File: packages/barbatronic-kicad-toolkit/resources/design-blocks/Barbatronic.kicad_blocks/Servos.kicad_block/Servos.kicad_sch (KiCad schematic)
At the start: 3 parts, among them J19 Conn_01x04

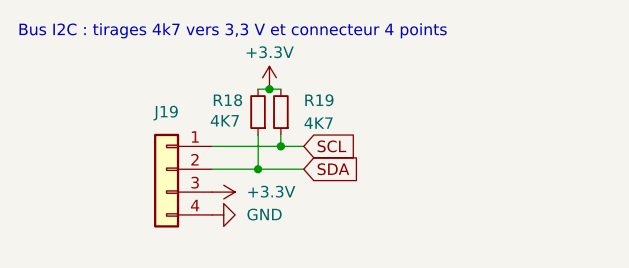
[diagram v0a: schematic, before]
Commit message: Sync docs with hand-edited design blocks
Entree_Alim_Protegee is gone, Servos_x4 is now the reusable single-
output Servos, and Regul_5V is new (78E05, needs the SparkFun PCM
power-symbols package for one symbol). Blocks are now maintained by
hand in KiCad, not generated.

Guard make_design_blocks.py behind --force: it wipes and rebuilds
the whole block library from a now-stale list, which would have
silently destroyed these edits on next run.
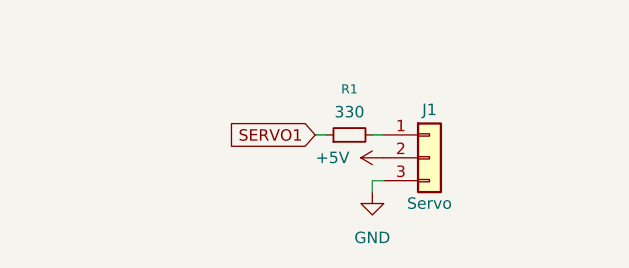
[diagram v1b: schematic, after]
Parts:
- removed J19: Conn_01x04, Connector_Molex:Molex_KK-254_AE-6410-04A_1x04_P2.54mm_Vertical, symbol Connector_Generic:Conn_01x04
- removed R18, R19: 4K7, Resistor_SMD:R_1206_3216Metric_Pad1.30x1.75mm_HandSolder, symbol Device:R_Small
- added J1: Servo, Connector_PinHeader_2.54mm:PinHeader_1x03_P2.54mm_Vertical, symbol Connector_Generic:Conn_01x03
- added R1: 330, Resistor_SMD:R_1206_3216Metric_Pad1.30x1.75mm_HandSolder, symbol Device:R_Small
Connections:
- net GND: now also J1.3 (Pin_3)
- new net: J1.1 (Pin_1), R1.2
- new net +5V: J1.2 (Pin_2)
- new net SERVO1: R1.1
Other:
- note removed: "Bus I2C : tirages 4k7 vers 3,3 V et connecteur 4 points"
